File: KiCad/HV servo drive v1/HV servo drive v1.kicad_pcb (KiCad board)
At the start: 4 copper layers, 138.2 x 199.5 mm, 360 parts, among them J1 PROG, J2 8P8C_LED_Shielded_x2, J3 Conn_02x03_Top_Bottom, J4 PFC SENSE, J5 MOTOR, J6 DC BUS J1, J7 DC BUS J2, M1 Fan_4pin, M2 Fan_4pin, Q1 PMOS, Q2 C3M0075120K, Q3 C3M0075120K, Q4 C3M0075120K, Q5 C3M0075120K, Q6 C3M0075120K, Q7 C3M0075120K, SW1 TERM RES, SW2 SW_DIP_x04, U1 PL133-37TC, U10 6N137, U11 6N137, U12 FODM217A, U13 FODM217A, U14 2EDF9275FXUMA1, U15 2EDF9275FXUMA1, U16 AMC1306M25DWVR, U17 AMC1306M25DWVR, U18 2EDF9275FXUMA1, U19 AMC1306M25DWVR, U2 STM32F413RGT6, U20 WRF0505S-3WR2, U21 B0505MT-1WR4, U22 B0505MT-1WR4, U23 TCA9555PWR, U3 AP2127K-3.3, U4 AP64060QWU-7, U5 THVD1552, U6 WRF0505S-3WR2, U7 ISO6721BQDRQ1, U8 ISO6721BQDRQ1, U9 ISO6721BQDRQ1

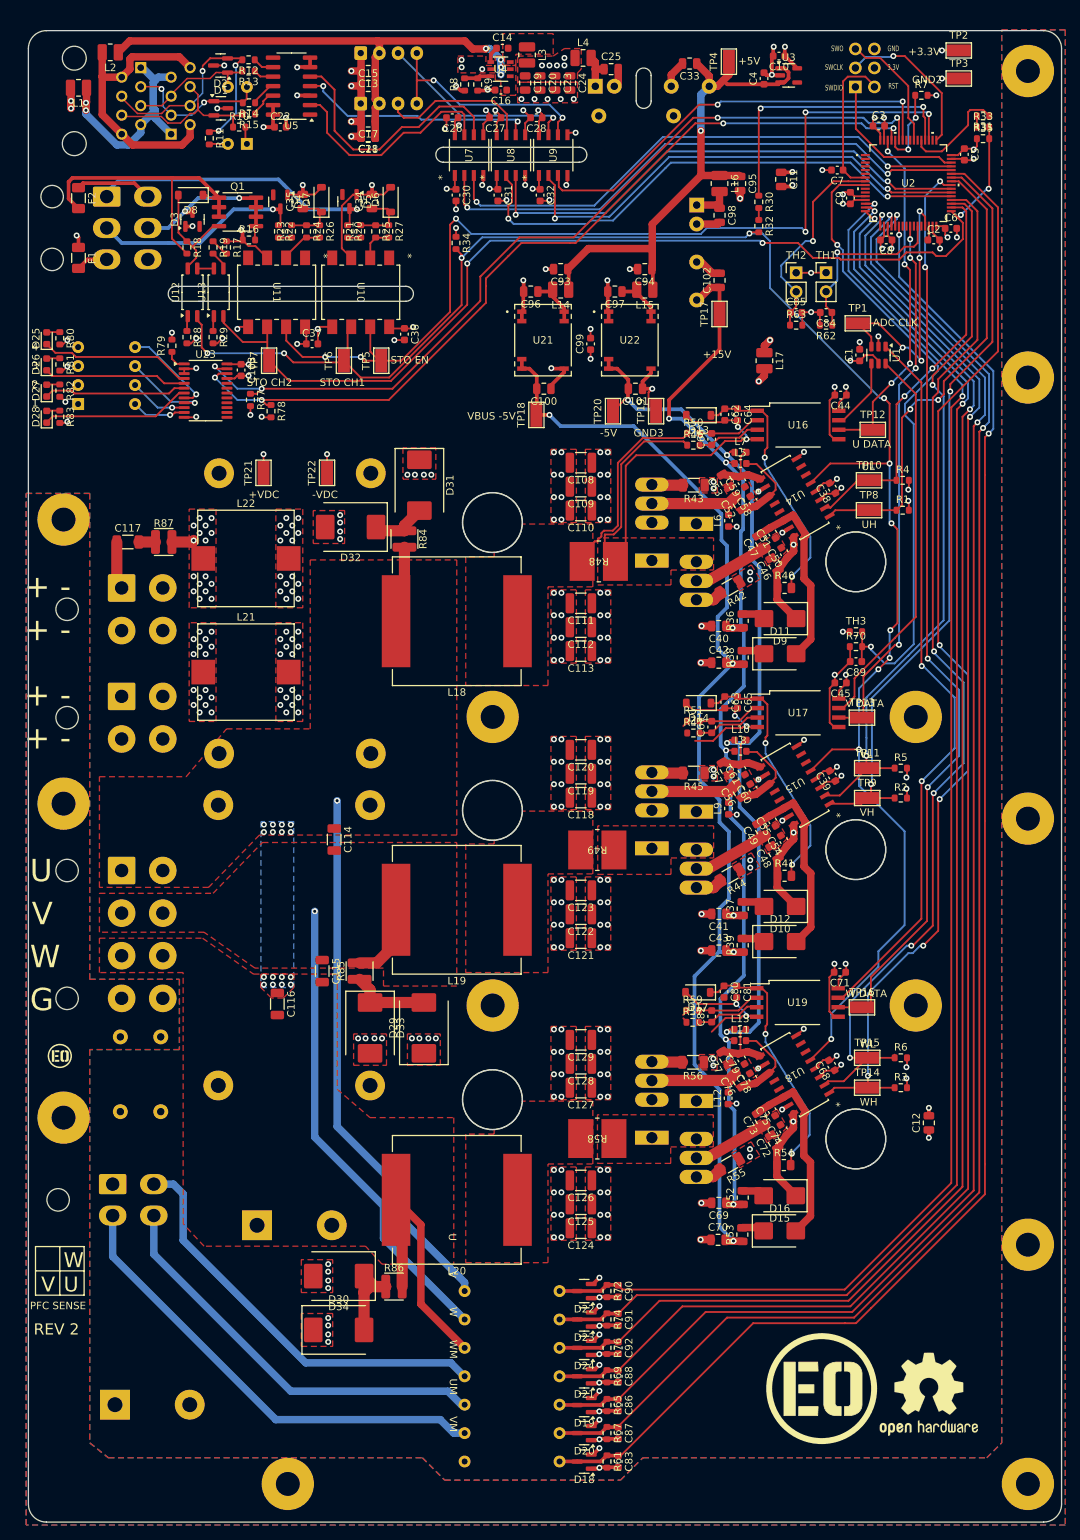
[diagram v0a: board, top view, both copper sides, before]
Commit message: update to rev 2.1
basically the same version as in the FOC youtube video, with some minor issues fixed
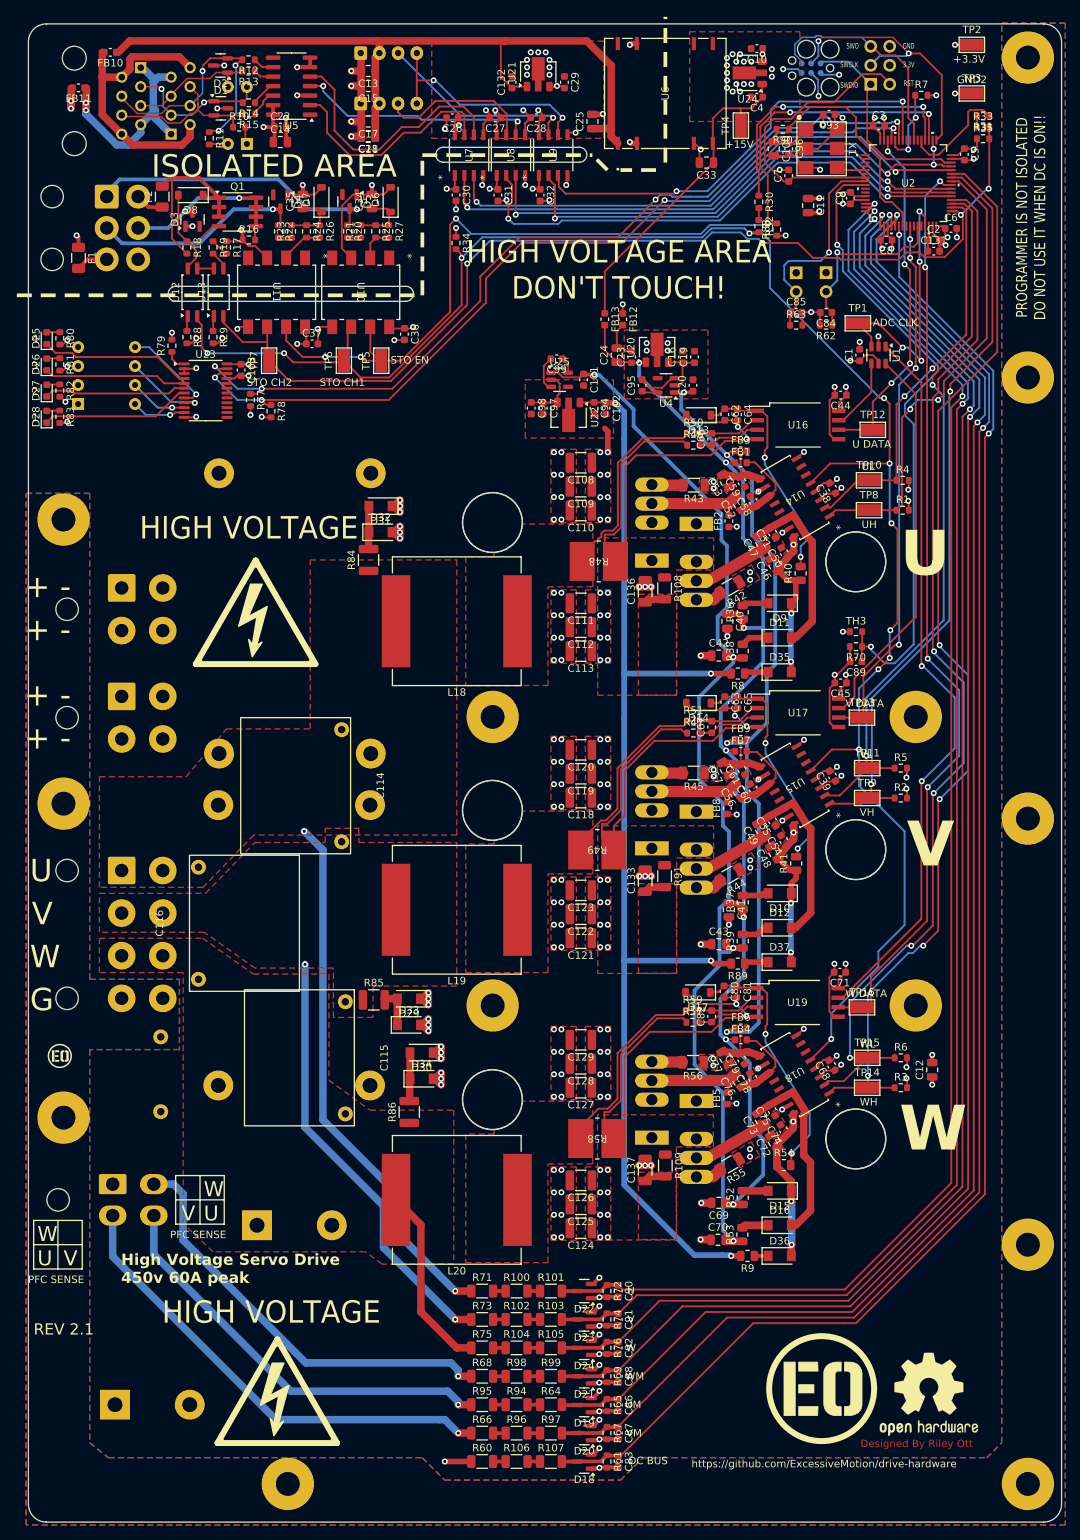
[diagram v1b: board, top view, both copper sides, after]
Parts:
- removed C117: 4.7nf, Capacitor_SMD:C_1206_3216Metric
- removed L1, L14, L15, L16, L17, L2, L3, L4: 10uH, Inductor_SMD:L_1008_2520Metric
- removed L10, L11, L12, L13, L5, L6, L7, L8, L9: 10uH, Inductor_SMD:L_0603_1608Metric
- removed L21, L22: 1uH, Inductor_SMD:L_Vishay_IHLP-5050
- removed R87: 4.7, footprints:R_1206_3216Metric_Wide
- removed TP17, TP18, TP19, TP20, TP21, TP22: TestPoint, footprints:TestPoint_Pad_3.1x1.6mm
- removed U3: AP2127K-3.3, Package_TO_SOT_SMD:SOT-23-5
- added C132: 0.1uf, Capacitor_SMD:C_0603_1608Metric, F.Cu at (375.0, 58.5)
- added C133: 470pf, Capacitor_SMD:C_1206_3216Metric, F.Cu at (392.8, 165.3)
- added C136: 470pf, Capacitor_SMD:C_1206_3216Metric, F.Cu at (392.8, 126.6)
- added C137: 470pf, Capacitor_SMD:C_1206_3216Metric, F.Cu at (392.8, 204.0)
- added D35: RS1MLW, footprints:D_SOD-123W, F.Cu at (410.8, 137.4)
- added D36: RS1MLW, footprints:D_SOD-123W, F.Cu at (410.8, 215.5)
- added D37: RS1MLW, footprints:D_SOD-123W, F.Cu at (410.8, 176.2)
- added FB1: 120 ohm, Inductor_SMD:L_0603_1608Metric, F.Cu at (405.6, 109.4)
- added FB10: 120 ohm, Inductor_SMD:L_0603_1608Metric, F.Cu at (321.2, 54.5)
- added FB11: 120 ohm, Inductor_SMD:L_0603_1608Metric, F.Cu at (317.0, 59.2)
- added FB12: 120 ohm, Inductor_SMD:L_0603_1608Metric, F.Cu at (389.8, 90.2)
- added FB13: 120 ohm, Inductor_SMD:L_0603_1608Metric, F.Cu at (387.4, 90.2)
- added FB2: 120 ohm, Inductor_SMD:L_0603_1608Metric, F.Cu at (404.0, 117.2)
- added FB3: 120 ohm, Inductor_SMD:L_0603_1608Metric, F.Cu at (405.6, 107.8)
- added FB4: 120 ohm, Inductor_SMD:L_0603_1608Metric, F.Cu at (405.6, 186.6)
- added FB5: 120 ohm, Inductor_SMD:L_0603_1608Metric, F.Cu at (403.8, 194.4)
- added FB6: 120 ohm, Inductor_SMD:L_0603_1608Metric, F.Cu at (405.6, 185.0)
- added FB7: 120 ohm, Inductor_SMD:L_0603_1608Metric, F.Cu at (405.6, 148.0)
- added FB8: 120 ohm, Inductor_SMD:L_0603_1608Metric, F.Cu at (403.8, 155.6)
- added FB9: 120 ohm, Inductor_SMD:L_0603_1608Metric, F.Cu at (405.6, 146.4)
- added J8: Conn_ARM_SWD_TagConnect_TC2030, Connector:Tag-Connect_TC2030-IDC-FP_2x03_P1.27mm_Vertical, B.Cu at (415.0, 56.6)
- added R100: 750k, Resistor_SMD:R_1206_3216Metric, F.Cu at (375.6, 220.2)
- added R101: 750k, Resistor_SMD:R_1206_3216Metric, F.Cu at (380.2, 220.2)
- added R102: 750k, Resistor_SMD:R_1206_3216Metric, F.Cu at (375.6, 224.0)
- added R103: 750k, Resistor_SMD:R_1206_3216Metric, F.Cu at (380.2, 224.0)
- added R104: 750k, Resistor_SMD:R_1206_3216Metric, F.Cu at (375.6, 227.8)
- added R105: 750k, Resistor_SMD:R_1206_3216Metric, F.Cu at (380.2, 227.8)
- added R106: 750k, Resistor_SMD:R_1206_3216Metric, F.Cu at (375.6, 243.0)
- added R107: 750k, Resistor_SMD:R_1206_3216Metric, F.Cu at (380.2, 243.0)
- added R108: 10, Resistor_SMD:R_1206_3216Metric, F.Cu at (395.4, 126.2)
- added R109: 10, Resistor_SMD:R_1206_3216Metric, F.Cu at (395.5, 203.4)
- added R88: 10k, Resistor_SMD:R_0603_1608Metric, F.Cu at (410.4, 78.2)
- added R89: 1, Resistor_SMD:R_0805_2012Metric, F.Cu at (405.2, 176.4)
- added R90: 1k, Resistor_SMD:R_0603_1608Metric, F.Cu at (411.2, 64.8)
- added R91: 10, Resistor_SMD:R_1206_3216Metric, F.Cu at (395.4, 164.7)
- added R94: 750k, Resistor_SMD:R_1206_3216Metric, F.Cu at (375.6, 235.4)
- added R95: 750k, Resistor_SMD:R_1206_3216Metric, F.Cu at (371.0, 235.4)
- added R96: 750k, Resistor_SMD:R_1206_3216Metric, F.Cu at (375.6, 239.2)
- added R97: 750k, Resistor_SMD:R_1206_3216Metric, F.Cu at (380.2, 239.2)
- added R98: 750k, Resistor_SMD:R_1206_3216Metric, F.Cu at (375.6, 231.6)
- added R99: 750k, Resistor_SMD:R_1206_3216Metric, F.Cu at (380.2, 231.6)
- added REF**: Symbol_HighVoltage_Triangle_17x15mm_Silk, footprints:Symbol_HighVoltage_Triangle_17x15mm_Silk, F.Cu at (340.7, 129.4)
- added REF**: Symbol_HighVoltage_Triangle_17x15mm_Silk, footprints:Symbol_HighVoltage_Triangle_17x15mm_Silk, F.Cu at (343.6, 233.6)
- added REF**: Symbol_HighVoltage_Triangle_17x15mm_Silk, footprints:Symbol_HighVoltage_Triangle_17x15mm_Silk, B.Cu at (426.5, 71.5)
- added REF**: Symbol_HighVoltage_Triangle_17x15mm_Silk, footprints:Symbol_HighVoltage_Triangle_17x15mm_Silk, B.Cu at (366.3, 233.2)
- added U24: AP2205-33Y-13, Package_TO_SOT_SMD:SOT-89-3, F.Cu at (406.5, 57.2)
- added U25: TPS60400DBV, Package_TO_SOT_SMD:SOT-23-5, F.Cu at (381.4, 98.3)
- added X1: FRETHE025, footprints:FR_3-3V, F.Cu at (416.4, 67.4)
- C10, C16, C4: value 2.2uf -> 0.1uf
- C101, C102, C19, C20, C95, C98: value 10uf -> 1uf; footprint Capacitor_SMD:C_0805_2012Metric -> Capacitor_SMD:C_0603_1608Metric
- C108, C109, C110, C111, C112, C113, C118, C119, C120, C121, C122, C123, C124, C125, C126, C127, C128, C129: value C -> 47nf
- C114, C115, C116: value 470pf -> 390pf; footprint Capacitor_SMD:C_1206_3216Metric -> footprints:B326712L-SMD
- C131: value 220pf -> 1uf; footprint Capacitor_THT:C_Disc_D7.5mm_W5.0mm_P10.00mm -> Capacitor_SMD:C_0603_1608Metric; moved to F.Cu
- C14: value .1uf -> 10uf; footprint Capacitor_SMD:C_0603_1608Metric -> Capacitor_SMD:C_0805_2012Metric
- C2, C84, C85, C89: value 2.2uf -> 1uf
- C23, C93, C94, C96, C97: value 10uf -> 0.1uf; footprint Capacitor_SMD:C_0805_2012Metric -> Capacitor_SMD:C_0603_1608Metric
- C29: value 220pf -> 0.1uf; footprint Capacitor_THT:C_Disc_D7.5mm_W5.0mm_P10.00mm -> Capacitor_SMD:C_0603_1608Metric; moved to F.Cu
- C62, C63, C80: value 2.2 -> 1uf
- C7: value .1uf -> 0.1uf
- C99: value 220pf -> 1uf
- D1, D2: value D_TVS_Dual_AAC -> SM712
- D10, D11, D12, D15, D16, D9: value D -> RS1MLW; footprint Diode_SMD:D_SMB -> footprints:D_SOD-123W
- D18, D19, D20, D21, D22, D23, D24, D3, D4, D5: value D_Dual_Series_ACK -> BAT54SLT1G
- D29, D30, D31, D32, D33, D34: value D -> RS1MLW; footprint Diode_SMD:D_SMC -> footprints:D_SOD-123W
- J2: value 8P8C_LED_Shielded_x2 -> E5908-0T0343-L
- J3: value Conn_02x03_Top_Bottom -> STO; footprint Connector_Molex:Molex_Mini-Fit_Jr_5569-06A2_2x03_P4.20mm_Horizontal -> footprints:Molex_Mini-Fit_Jr_0455580003_2x03_P4.20mm_Horizontal
- J6: value DC BUS J1 -> DC BUS
- J7: value DC BUS J2 -> DC BUS
- L18, L19, L20: value 1uH -> 3.3uH
- Q1: value PMOS -> AO4421
- Q2, Q3, Q4, Q5, Q6, Q7: value C3M0075120K -> G3R30MT12K
- R16, R18, R30, R31, R32, R33: value 10K -> 10k
- R17, R19, R20, R21, R22, R23, R34, R35: value 1K -> 1k
- R40, R41, R54: value 800 -> 820
- R46, R47, R50, R51, R57, R59: value R -> 0
- R60, R64, R66, R68, R71, R73, R75: value 1M -> 750k; footprint Resistor_THT:R_Axial_DIN0309_L9.0mm_D3.2mm_P12.70mm_Horizontal -> Resistor_SMD:R_1206_3216Metric; moved to F.Cu
- R61, R65, R67, R69, R72, R74, R76: value 5k -> 10k
- R8: value 115k -> 1; footprint Resistor_SMD:R_0603_1608Metric -> Resistor_SMD:R_0805_2012Metric
- R84, R85, R86: value 4.7 -> 20; footprint footprints:R_1206_3216Metric_Wide -> Resistor_SMD:R_1210_3225Metric
- R9: value 22.1k -> 1; footprint Resistor_SMD:R_0603_1608Metric -> Resistor_SMD:R_0805_2012Metric
- SW1: value TERM RES -> DS01-254-L-02BE
- SW2: value SW_DIP_x04 -> DS02C-254-1L-04BE
- TH1, TH2: moved to B.Cu
- U12, U13: value FODM217A -> EL3H7
- U14, U15, U18: value 2EDF9275FXUMA1 -> 2EDF8275FXUMA1
- U20: value WRF0505S-3WR2 -> AP2205-50Y-13; footprint footprints:B0515 -> Package_TO_SOT_SMD:SOT-89-3; moved to F.Cu
- U21, U22: value B0505MT-1WR4 -> AP2205-50Y-13; footprint footprints:B05xxMT-1WR4_MNS -> Package_TO_SOT_SMD:SOT-89-3
- U4: value AP64060QWU-7 -> TPS60400DBV; footprint footprints:IC6_AP64060QWU-7_DIO -> Package_TO_SOT_SMD:SOT-23-5
- U5: value THVD1552 -> THVD1552DR
- U6: value WRF0505S-3WR2 -> NXJ2S2415MC-R7; footprint footprints:F0505S-2WR3 -> footprints:NXJ2_24V_MUR; moved to F.Cu
- moved R9 160.8 mm to (406.5, 215.5), turned to 180 degrees
- moved C131 151.3 mm to (431.4, 81.1), turned to 0 degrees
- moved R8 86.9 mm to (405.2, 137.6), turned to 180 degrees
- moved U4 47.7 mm to (395.6, 99.0), turned to 180 degrees
- moved C20 45.3 mm to (399.2, 99.0), turned to 90 degrees
- moved C100 44.5 mm to (410.0, 67.4), turned to -90 degrees
- moved C16 43.2 mm to (397.8, 95.2), turned to 90 degrees
- moved C19 43.1 mm to (399.4, 95.2), turned to 90 degrees
- moved C93 41.4 mm to (417.4, 62.8)
- moved C96 39.4 mm to (412.0, 67.4), turned to -90 degrees
- moved D30 38.7 mm to (362.9, 188.3), turned to 180 degrees
- moved C23 38.1 mm to (391.0, 95.2), turned to 90 degrees
- moved C24 36.9 mm to (389.0, 95.0), turned to 90 degrees
- moved C98 36.1 mm to (377.6, 102.1)
- moved U21 35.9 mm to (378.5, 57.1), turned to 90 degrees
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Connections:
- C100 pad 1: +VDC -> Net-(X1-VC)
- C100 pad 2: VBUS -5V -> GND2
- C101 pad 1: GND3 -> VBUS -5V
- C101 pad 2: -5V -> DCBUS+
- C102 pad 1: +15V -> VBUS +15V
- C102 pad 2: GND3 -> DCBUS+
- C104 pad 1: +VDC -> DCBUS+
- C104 pad 2: -VDC -> DCBUS-
- C105 pad 1: +VDC -> DCBUS+
- C105 pad 2: -VDC -> DCBUS-
- C106 pad 1: +VDC -> DCBUS+
- C106 pad 2: -VDC -> DCBUS-
- C107 pad 1: +VDC -> DCBUS+
- C107 pad 2: -VDC -> DCBUS-
- C108 pad 1: +VDC -> DCBUS+
- C108 pad 2: -VDC -> DCBUS-
- C109 pad 1: +VDC -> DCBUS+
- C109 pad 2: -VDC -> DCBUS-
- C110 pad 1: +VDC -> DCBUS+
- C110 pad 2: -VDC -> DCBUS-
- C111 pad 1: +VDC -> DCBUS+
- C111 pad 2: -VDC -> DCBUS-
- C112 pad 1: +VDC -> DCBUS+
- C112 pad 2: -VDC -> DCBUS-
- C113 pad 1: +VDC -> DCBUS+
- C113 pad 2: -VDC -> DCBUS-
- C114 pad 1: U -> V
- C114 pad 2: V -> U
- C115 pad 1: V -> W
- C115 pad 2: W -> V
- C118 pad 1: +VDC -> DCBUS+
- C118 pad 2: -VDC -> DCBUS-
- C119 pad 1: +VDC -> DCBUS+
- C119 pad 2: -VDC -> DCBUS-
- C120 pad 1: +VDC -> DCBUS+
- C120 pad 2: -VDC -> DCBUS-
- C121 pad 1: +VDC -> DCBUS+
- C121 pad 2: -VDC -> DCBUS-
- C122 pad 1: +VDC -> DCBUS+
- C122 pad 2: -VDC -> DCBUS-
- C123 pad 1: +VDC -> DCBUS+
- C123 pad 2: -VDC -> DCBUS-
- C124 pad 1: +VDC -> DCBUS+
- C124 pad 2: -VDC -> DCBUS-
- C125 pad 1: +VDC -> DCBUS+
- C125 pad 2: -VDC -> DCBUS-
- C126 pad 1: +VDC -> DCBUS+
- C126 pad 2: -VDC -> DCBUS-
- C127 pad 1: +VDC -> DCBUS+
- C127 pad 2: -VDC -> DCBUS-
- C128 pad 1: +VDC -> DCBUS+
- C128 pad 2: -VDC -> DCBUS-
- C129 pad 1: +VDC -> DCBUS+
- C129 pad 2: -VDC -> DCBUS-
- C130 pad 2: -VDC -> DCBUS-
- C131 pad 1: GND -> Net-(U2A-VCAP_1)
- C131 pad 2: +VDC -> GND2
- C14 pad 1: Net-(U4-BST) -> 5v_ISO
- C14 pad 2: Net-(U4-SW) -> GND1
- C16 pad 1: 24V_ISO -> Net-(U20-VOUT)
- C16 pad 2: GND1 -> GND3
- C19 pad 1: 5v_ISO -> Net-(U20-VOUT)
- C19 pad 2: GND1 -> GND3
- C20 pad 1: 5v_ISO -> -5V
- C20 pad 2: GND1 -> GND3
- C23 pad 1: 5v_ISO -> +15V_GATE
- C23 pad 2: GND1 -> GND3
- C24 pad 1: 5v_ISO -> +15V_GATE
- C24 pad 2: GND1 -> GND3
- C25 pad 1: Net-(U6-VIN) -> 24V_ISO
- C29 pad 1: GND2 -> GND1
- C29 pad 2: GND1 -> 5v_ISO
- C33 pad 1: +5V -> +15V
- C4 pad 1: +5V -> +15V
- C40 pad 1: +15V -> +15V_GATE
- C41 pad 1: +15V -> +15V_GATE
- C42 pad 1: +VDC -> DCBUS+
- C43 pad 1: +VDC -> DCBUS+
- C69 pad 1: +15V -> +15V_GATE
- C70 pad 1: +VDC -> DCBUS+
- C93 pad 1: +5V -> +3.3V
- C94 pad 1: +5V -> VBUS +15V
- C94 pad 2: GND2 -> DCBUS+
- C95 pad 1: +5V -> Net-(U4-C_{FLY+})
- C95 pad 2: GND2 -> Net-(U4-C_{FLY-})
- C96 pad 1: Net-(C96-Pad1) -> Net-(X1-VC)
- C97 pad 1: Net-(C97-Pad1) -> Net-(U22-VOUT)
- C97 pad 2: GND2 -> DCBUS+
- C98 pad 1: Net-(U20-VIN) -> Net-(U22-VOUT)
- C98 pad 2: GND2 -> DCBUS+
- C99 pad 1: GND3 -> Net-(U25-C_{FLY+})
- C99 pad 2: GND2 -> Net-(U25-C_{FLY-})
- D29 pad 1: +VDC -> DCBUS+
- D30 pad 1: +VDC -> DCBUS+
- D31 pad 1: +VDC -> DCBUS+
- D32 pad 2: -VDC -> DCBUS-
- D33 pad 2: -VDC -> DCBUS-
- D34 pad 2: -VDC -> DCBUS-
- Q2 pad 1: +VDC -> DCBUS+
- Q3 pad 2: -VDC -> DCBUS-
- Q4 pad 1: +VDC -> DCBUS+
- Q5 pad 2: -VDC -> DCBUS-
- Q6 pad 1: +VDC -> DCBUS+
- Q7 pad 2: -VDC -> DCBUS-
- R36 pad 1: +15V -> +15V_GATE
- R37 pad 1: +15V -> +15V_GATE
- R52 pad 1: +15V -> +15V_GATE
- R60 pad 1: +VDC -> DCBUS+
- R60 pad 2: VBUS_ADC -> Net-(R106-Pad1)
- R64 pad 1: UM -> Net-(R64-Pad1)
- R66 pad 2: VM_ADC -> Net-(R66-Pad2)
- R68 pad 2: WM_ADC -> Net-(R68-Pad2)
- R71 pad 2: U_ADC -> Net-(R100-Pad1)
- R73 pad 2: V_ADC -> Net-(R102-Pad1)
- R75 pad 2: W_ADC -> Net-(R104-Pad1)
- R8 pad 1: 5v_ISO -> Net-(D35-K)
- R8 pad 2: Net-(U4-FB) -> VBUS +15V
- R84 pad 1: Net-(D31-A) -> U
- R84 pad 2: U -> Net-(D31-A)
- R85 pad 1: Net-(D29-A) -> V
- R85 pad 2: V -> Net-(D29-A)
- R86 pad 1: Net-(D30-A) -> W
- R86 pad 2: W -> Net-(D30-A)
- R9 pad 1: Net-(U4-FB) -> Net-(D36-K)
- R9 pad 2: GND1 -> VBUS +15V
- TP4 pad 1: +5V -> +15V
- U2 pad 23: GATE_SUPPLY_ADC -> VCXO_VC
- U2 pad 44: RX -> TX
- U2 pad 45: TX -> RX
- U2 pad 5: unconnected-(U2B-PH0-OSC_IN-Pad5) -> OSC
- U2 pad 50: unconnected-(U2B-PA15-Pad50) -> RX
- U20 pad 1: Net-(U20-VIN) -> +15V_GATE
- U20 pad 2: GND2 -> GND3
- U21 pad 1: GND2 -> 24V_ISO
- U21 pad 2: GND2 -> GND1
- U22 pad 1: GND2 -> VBUS +15V
- U22 pad 2: GND2 -> DCBUS+
- U4 pad 1: Net-(U4-BST) -> -5V
- U4 pad 2: GND1 -> Net-(U20-VOUT)
- U4 pad 3: Net-(U4-FB) -> Net-(U4-C_{FLY-})
- U4 pad 4: 24V_ISO -> GND3
- U4 pad 5: 24V_ISO -> Net-(U4-C_{FLY+})
- U6 pad 1: Net-(U6-VIN) -> 24V_ISO
- U6 pad 7: +5V -> unconnected-(U6-NC-Pad7)
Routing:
- net VBUS +15V: track 0.00 -> 158.1 mm, vias 0 -> 4
- net +15V_GATE: track 0.00 -> 153.5 mm, vias 0 -> 7
- net +15V: track 153.0 -> 44.1 mm, vias 7 -> 0
- net +5V: track 71.2 -> 0.00 mm, vias 1 -> 0
- net Net-(D17-A): track 18.1 -> 67.7 mm
- net Net-(D14-A): track 19.5 -> 65.9 mm
- net 24V_ISO: track 68.5 -> 104.3 mm, vias 4 -> 0
- net VCXO_VC: track 0.00 -> 28.6 mm
- net +VDC: track 28.4 -> 0.00 mm, vias 81 -> 0
- net W_: track 0.87 -> 25.9 mm
- net V_: track 0.87 -> 25.4 mm
- net RESET: track 20.3 -> 44.0 mm, vias 0 -> 1
- net DCBUS-: track 2.98 -> 24.2 mm, vias 16 -> 66
- net DCBUS+: track 6.42 -> 24.8 mm, vias 16 -> 61
- net STO FBK 24V: track 41.4 -> 25.0 mm
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- added copper zone on F.Cu, net GND2
- added copper zone on F.Cu, net GND3
- added copper zone on F.Cu, net Net-(C133-Pad1)
- added copper zone on F.Cu, net Net-(C136-Pad1)
- added copper zone on F.Cu, net Net-(C137-Pad1)
- removed copper zone on F.Cu, net (none)
- removed copper zone on F.Cu, net +VDC
- removed copper zone on In1.Cu, net +VDC
- removed copper zone on F.Cu, net -VDC
- removed copper zone on In2.Cu, net -VDC
- removed copper zone on F.Cu, net 24V_ISO
- removed copper zone on F.Cu, net 5v_ISO
- removed copper zone on B.Cu, net U
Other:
- board size 138.2 x 199.5 mm -> 138.2 x 200.4 mm
- board text added: "24V"
- board text added: "DC BUS"
- board text added: "Designed By Riley Ott"
- board text added: "FAN1"
- board text added: "FAN2"
- board text added: "HIGH VOLTAGE"
- board text added: "HIGH VOLTAGE AREA DON'T TOUCH!"
- board text added: "High Voltage Servo Drive 450v 60A peak"
- board text added: "ISOLATED AREA"
- board text added: "PROGRAMMER IS NOT ISOLATED DO NOT USE IT WHEN DC IS ON!!"
- board text added: "PWM"
- board text added: "REV 2.1"
- board text added: "TACH"
- board text added: "THERM 1"
- board text added: "THERM 2"
- board text added: "https://github.com/ExcessiveMotion/drive-hardware"
- board text removed: "+5V"
- board text removed: "+VDC"
- board text removed: "-5V"
- board text removed: "-VDC"
- board text removed: "GND3"
- board text removed: "REV 2"
- board text removed: "VBUS -5V"

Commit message: add reverse protection diodes to gate supply
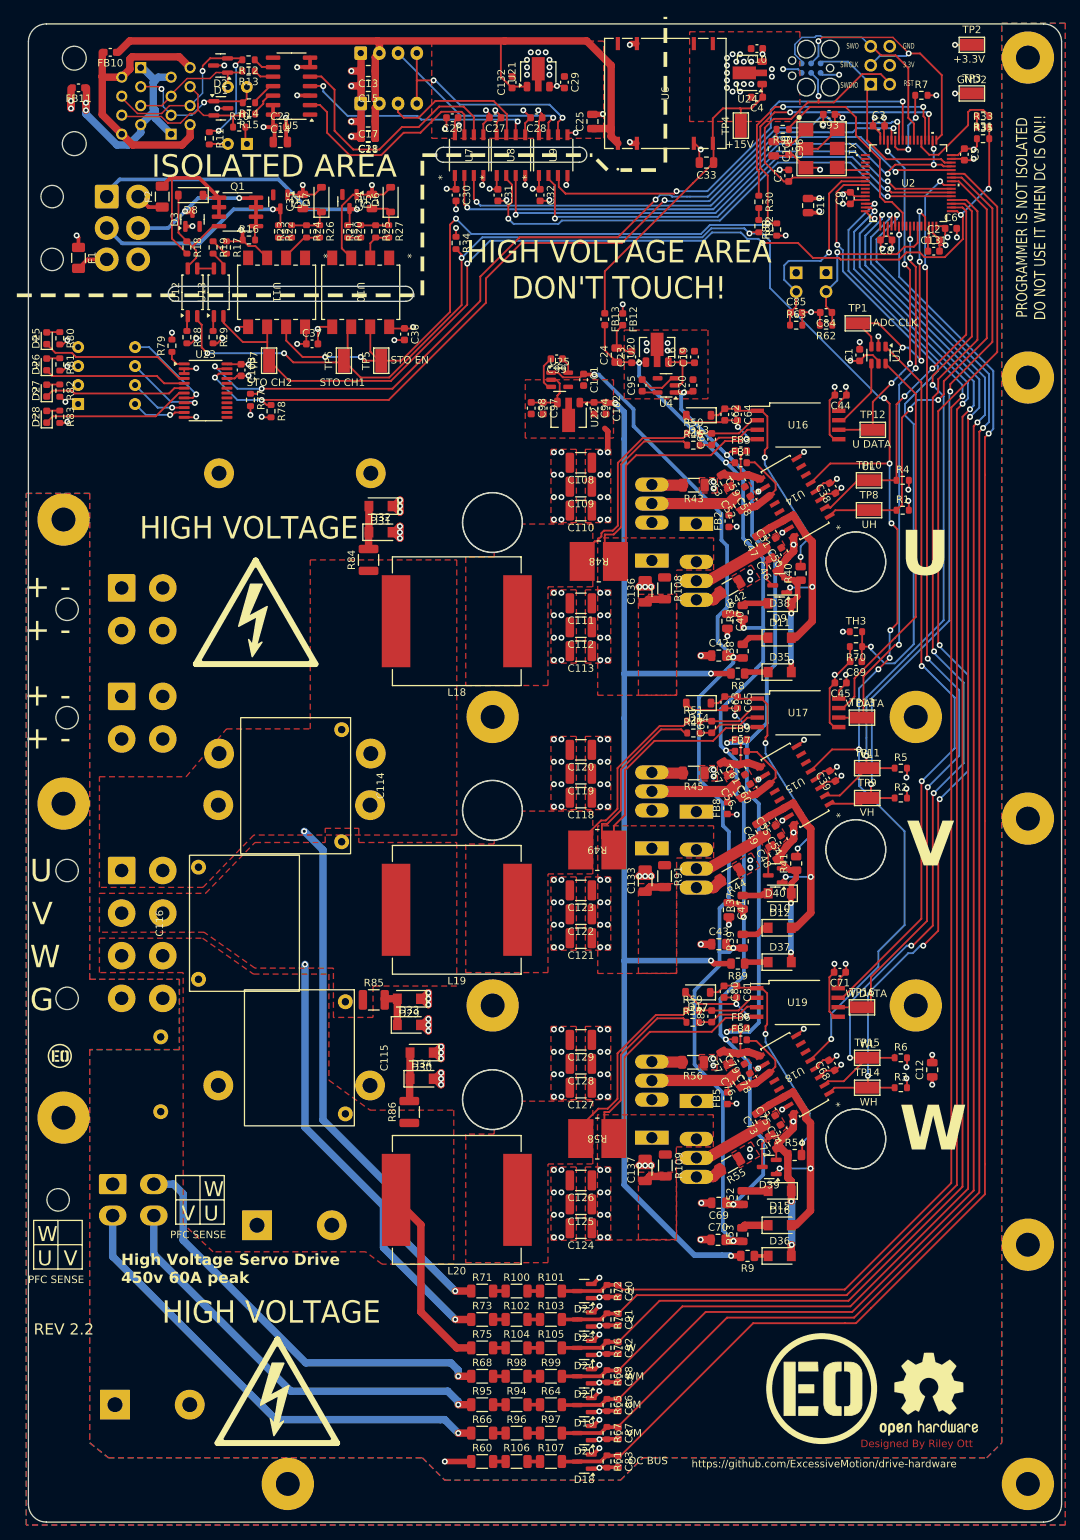
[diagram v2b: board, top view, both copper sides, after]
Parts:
- added D38: BAT54SLT1G, Package_TO_SOT_SMD:SOT-23, F.Cu at (410.8, 125.8)
- added D39: BAT54SLT1G, Package_TO_SOT_SMD:SOT-23, F.Cu at (409.4, 203.6)
- added D40: BAT54SLT1G, Package_TO_SOT_SMD:SOT-23, F.Cu at (410.2, 164.6)
- moved R54 1.98 mm to (412.8, 202.0)
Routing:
- net Net-(D16-A): track 25.2 -> 30.1 mm, vias 0 -> 2
- net Net-(D39-common): track 9.12 -> 13.8 mm
- net Net-(D12-A): track 23.9 -> 28.2 mm, vias 0 -> 2
- net Net-(D38-common): track 9.12 -> 13.3 mm
- net Net-(D40-common): track 9.12 -> 13.2 mm
- net Net-(D11-A): track 23.8 -> 27.6 mm, vias 0 -> 2
- net Net-(D17-K): track 34.1 -> 32.2 mm
- net Net-(D15-K): track 20.7 -> 22.5 mm
- net Net-(D10-K): track 20.5 -> 21.2 mm
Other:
- board text added: "REV 2.2"
- board text removed: "REV 2.1"
